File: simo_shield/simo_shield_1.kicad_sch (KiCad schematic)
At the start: 8 parts, among them J1 modulo_usb_debug, J2 conector_bateria, U1 modulo_flash_externa, U2 elemon_board, U3 bluepill_board_stm32, U4 modulo_acelerometro

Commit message: update en simo_bateria
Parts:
- J2: footprint Connector_JST:JST_EH_B2B-EH-A_1x02_P2.50mm_Vertical -> simo_shield:JST_EH_B2B-EH-A_1x02_P2.50mm_Vertical
- U1: footprint simo_board:conector_flash_ext -> simo_shield:conector_flash_ext
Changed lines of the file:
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@@
     (property "Reference" "U1" (id 0) (at 35.56 151.257 0))
     (property "Value" "modulo_flash_externa" (id 1) (at 35.56 153.797 0))
-    (property "Footprint" "simo_board:conector_flash_ext" (id 2) (at 48.26 156.972 0)
+    (property "Footprint" "simo_shield:conector_flash_ext" (id 2) (at 48.26 156.972 0)
       (effects (font (size 1.27 1.27)) hide)
     )
@@
       (effects (font (size 1.27 1.27)) (justify left))
     )
-    (property "Footprint" "Connector_JST:JST_EH_B2B-EH-A_1x02_P2.50mm_Vertical" (id 2) (at 243.967 108.458 0)
+    (property "Footprint" "simo_shield:JST_EH_B2B-EH-A_1x02_P2.50mm_Vertical" (id 2) (at 243.967 108.458 0)
       (effects (font (size 1.27 1.27)) hide)
     )
@@
     )
     (path "/aa8a4ce4-263f-4980-8d9f-4f0f7a62a8f5"
-      (reference "J2") (unit 1) (value "conector_bateria") (footprint "Connector_JST:JST_EH_B2B-EH-A_1x02_P2.50mm_Vertical")
+      (reference "J2") (unit 1) (value "conector_bateria") (footprint "simo_shield:JST_EH_B2B-EH-A_1x02_P2.50mm_Vertical")
     )
     (path "/50ab3c25-18ac-4348-9b10-e46fc412d281"
-      (reference "U1") (unit 1) (value "modulo_flash_externa") (footprint "simo_board:conector_flash_ext")
+      (reference "U1") (unit 1) (value "modulo_flash_externa") (footprint "simo_shield:conector_flash_ext")
     )
     (path "/4e546ac2-24a9-4fe8-8ba3-1b8a7c4f035f"

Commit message: update en ambas placas, revision 02
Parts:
- removed 155k1, 365k1: R, simo_shield:R_0805_2012Metric, symbol simo_shield:R
- removed U2: elemon_board, simo_shield:elemon_board, symbol simo_shield:elemon_board
- added U1: elemon_board, simo_shield:elemon_board, symbol simo_shield:elemon_board
- renumbered U1 to U2
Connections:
- net BAT_LEVEL is gone; now on an unnamed net: U3.25 (PA0)
- net BAT_ENA_PIN: now also U1.52 (BAT_ENA)
- net BAT_GND: now also U1.10 (GND)
- net GND_ELEMON: now also U3.41 (GND), U1.24 (GND)
- net UART_DEBUG_RX: now also U3.27 (PA2); no longer U3.28 (PA3)
- net UART_DEBUG_TX: now also U3.28 (PA3); no longer U3.27 (PA2)
- net USB33_ELEMON: now also U3.44 (3V3), U1.23 (USB33)
- net at U3.10 (PA15): now also U1.14 (RI)
- net at U3.7 (PA10): now also U1.2 (SER3_TX)
- net at U3.6 (PA9): now also U1.4 (SER3_RX)
- net at U3.2 (PB13): now also U1.9 (PWRKEY)
- no-connect marks 78 -> 76
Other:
- note added: "La tension en el conector es siempre menor a 3.3v"
- note removed: "0,30 * VBAT (8V MAX)"
- note removed: "ESTE PUENTE DEPENDE DE SI USAMOS 1 O DOS BATERIAS EN SERIE"
- moved on the sheet: J1, J2, U2, U3, U4

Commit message: update 2. Listo para revision 2
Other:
- note added: "La tension en el conector es siempre menor a 3.3v. PA0 canal analogico utilizado."
- note removed: "La tension en el conector es siempre menor a 3.3v"
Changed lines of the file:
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@@
   (junction (at 177.8 64.77) (diameter 0) (color 0 0 0 0)
-  )
-  (junction (at 217.17 100.33) (diameter 0) (color 0 0 0 0)
   )
   (junction (at 124.46 110.49) (diameter 0) (color 0 0 0 0)
@@
     (stroke (width 0) (type default) (color 0 0 0 0))
   )
-  (wire (pts (xy 173.99 100.33) (xy 217.17 100.33))
-    (stroke (width 0) (type default) (color 0 0 0 0))
-  )
   (wire (pts (xy 173.99 72.39) (xy 223.52 72.39))
     (stroke (width 0) (type default) (color 0 0 0 0))
@@
     (stroke (width 0) (type default) (color 0 0 0 0))
   )
-  (wire (pts (xy 217.17 99.06) (xy 217.17 100.33))
-    (stroke (width 0) (type default) (color 0 0 0 0))
-  )
   (polyline (pts (xy 283.21 40.64) (xy 283.21 83.82))
     (stroke (width 0) (type default) (color 0 0 0 0))
@@
     (stroke (width 0) (type default) (color 0 0 0 0))
   )
-  (wire (pts (xy 217.17 100.33) (xy 218.44 100.33))
+  (wire (pts (xy 173.99 100.33) (xy 218.44 100.33))
     (stroke (width 0) (type default) (color 0 0 0 0))
   )
@@
     (effects (font (size 1.27 1.27)) (justify left bottom))
   )
-  (text "La tension en el conector es siempre menor a 3.3v" (at 209.55 92.71 0)
+  (text "La tension en el conector es siempre menor a 3.3v.\nPA0 canal analogico utilizado."
+    (at 209.55 92.71 0)
     (effects (font (size 1.27 1.27)) (justify left bottom))
   )
@@
   (label "GND_ELEMON" (at 177.8 59.69 0)
     (effects (font (size 1.27 1.27)) (justify left bottom))
-  )
-  (symbol (lib_id "simo_shield:PWR_FLAG") (at 217.17 99.06 0) (unit 1)
-    (in_bom yes) (on_board yes)
-    (property "Reference" "#FLG01" (id 0) (at 217.17 97.155 0)
-      (effects (font (size 1.27 1.27)) hide)
-    )
-    (property "Value" "PWR_FLAG" (id 1) (at 217.17 95.25 0))
-    (property "Footprint" "" (id 2) (at 217.17 99.06 0)
-      (effects (font (size 1.27 1.27)) hide)
-    )
-    (property "Datasheet" "~" (id 3) (at 217.17 99.06 0)
-      (effects (font (size 1.27 1.27)) hide)
-    )
-    (pin "1")
   )
   (symbol (lib_id "simo_shield:modulo_flash_externa") (at 52.07 157.48 0) (mirror y) (unit 1)
@@
   )
   (symbol_instances
-    (path "/3bcc8c84-3847-43a1-a408-156ef3b78686"
-      (reference "#FLG01") (unit 1) (value "PWR_FLAG") (footprint "")
-    )
     (path "/fc6149f3-6c8e-44e2-b6f1-cd1c7ffb6984"
       (reference "J1") (unit 1) (value "modulo_usb_debug") (footprint "simo_shield:JST_EH_B2B-EH-A_1x02_P2.50mm_Vertical")

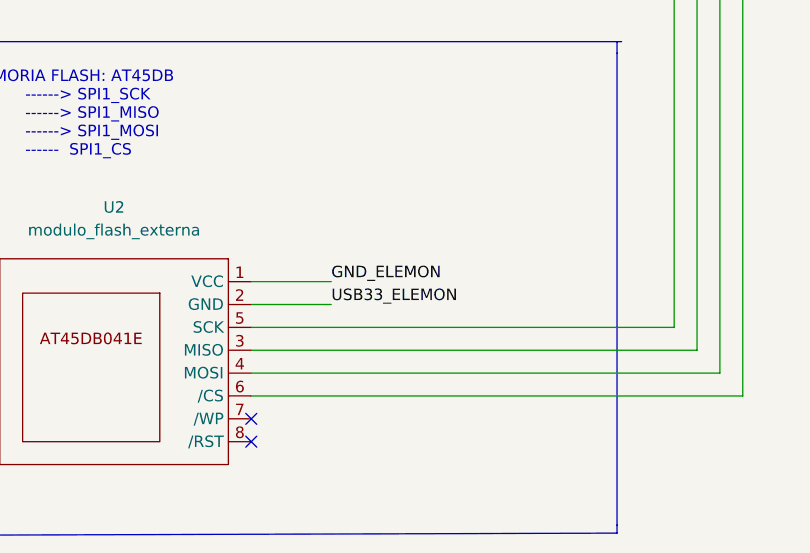
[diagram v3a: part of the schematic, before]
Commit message: modificaciones en simo_shield: modulo_flash_externo
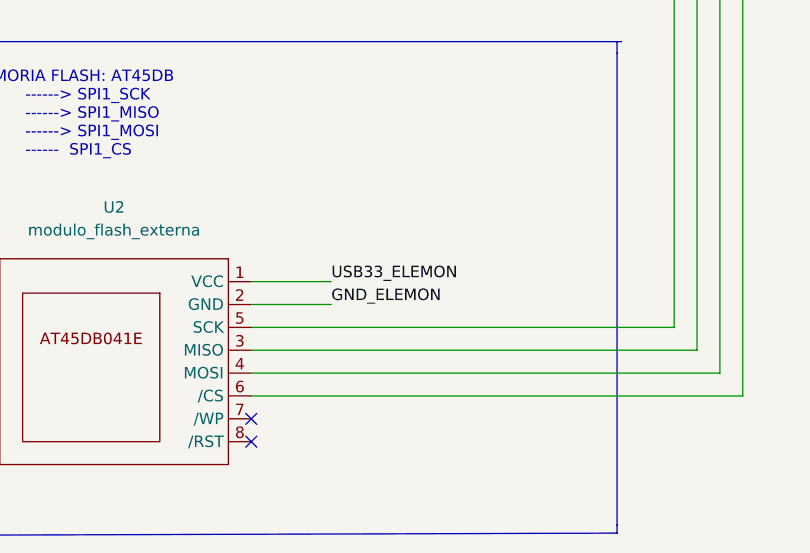
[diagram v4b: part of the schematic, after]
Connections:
- net GND_ELEMON: now also U2.2 (GND); no longer U2.1 (VCC)
- net USB33_ELEMON: now also U2.1 (VCC); no longer U2.2 (GND)
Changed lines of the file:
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@@
     (effects (font (size 1.27 1.27)) (justify right bottom))
   )
-  (label "GND_ELEMON" (at 63.5 160.02 0)
+  (label "GND_ELEMON" (at 63.5 162.56 0)
     (effects (font (size 1.27 1.27)) (justify left bottom))
   )
@@
     (effects (font (size 1.27 1.27)) (justify right bottom))
   )
-  (label "USB33_ELEMON" (at 63.5 162.56 0)
+  (label "USB33_ELEMON" (at 63.5 160.02 0)
     (effects (font (size 1.27 1.27)) (justify left bottom))
   )

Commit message: comenzamos el diseño del PCB de shield simo.
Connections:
- net at U1.14 (RI): now also U3.9 (PA12); no longer U3.10 (PA15)
- net at U1.9 (PWRKEY): now also U3.8 (PA11); no longer U3.2 (PB13)
- no-connect marks 76 -> 75
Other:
- note added: "ELEMON BOARD: BASADA EN SIM7000G PIN_SIM_ENA_BAT -------> PA1 (EN FIRMWARE ES PB12. MODIFICAR) PIN_SIM_PWRUP -------> PA11 (EN FIRMWARE ES PB13) PIN_AT_TX -------> PA10 PIN_AT_RX -------> PA9 PIN_RI -------> PA11"
- note removed: "ELEMON BOARD: BASADA EN SIM7000G PIN_SIM_ENA_BAT -------> PA1 (EN FIRMWARE ES PB12. MODIFICAR) PIN_SIM_PWRUP -------> PB13 PIN_AT_TX -------> PA10 PIN_AT_RX -------> PA9 PIN_RI -------> PA15"
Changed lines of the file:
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@@
   )
   (no_connect (at 127 69.85))
-  (no_connect (at 127 77.47))
   (no_connect (at 127 80.01))
   (no_connect (at 127 67.31))
@@
     (stroke (width 0) (type default) (color 0 0 0 0))
   )
+  (wire (pts (xy 127 77.47) (xy 101.6 77.47))
+    (stroke (width 0) (type default) (color 0 0 0 0))
+  )
   (wire (pts (xy 124.46 110.49) (xy 127 110.49))
     (stroke (width 0) (type default) (color 0 0 0 0))
@@
     (stroke (width 0) (type default) (color 0 0 0 0))
   )
+  (wire (pts (xy 101.6 77.47) (xy 101.6 62.23))
+    (stroke (width 0) (type default) (color 0 0 0 0))
+  )
   (wire (pts (xy 106.68 90.17) (xy 127 90.17))
     (stroke (width 0) (type default) (color 0 0 0 0))
@@
     (stroke (width 0) (type default) (color 0 0 0 0))
   )
-  (wire (pts (xy 67.31 62.23) (xy 127 62.23))
+  (wire (pts (xy 67.31 62.23) (xy 101.6 62.23))
     (stroke (width 0) (type default) (color 0 0 0 0))
   )
@@
     (effects (font (size 1.27 1.27)) (justify left bottom))
   )
-  (text "ELEMON BOARD: BASADA EN SIM7000G\n\nPIN_SIM_ENA_BAT    -------> PA1 (EN FIRMWARE ES PB12. MODIFICAR)\nPIN_SIM_PWRUP     -------> PB13\nPIN_AT_TX	     -------> PA10\nPIN_AT_RX	     -------> PA9\nPIN_RI			-------> PA15"
+  (text "ELEMON BOARD: BASADA EN SIM7000G\n\nPIN_SIM_ENA_BAT    -------> PA1 (EN FIRMWARE ES PB12. MODIFICAR)\nPIN_SIM_PWRUP     -------> PA11 (EN FIRMWARE ES PB13)\nPIN_AT_TX	     -------> PA10\nPIN_AT_RX	     -------> PA9\nPIN_RI			-------> PA11"
     (at 18.415 34.29 0)
     (effects (font (size 1.27 1.27)) (justify left bottom))

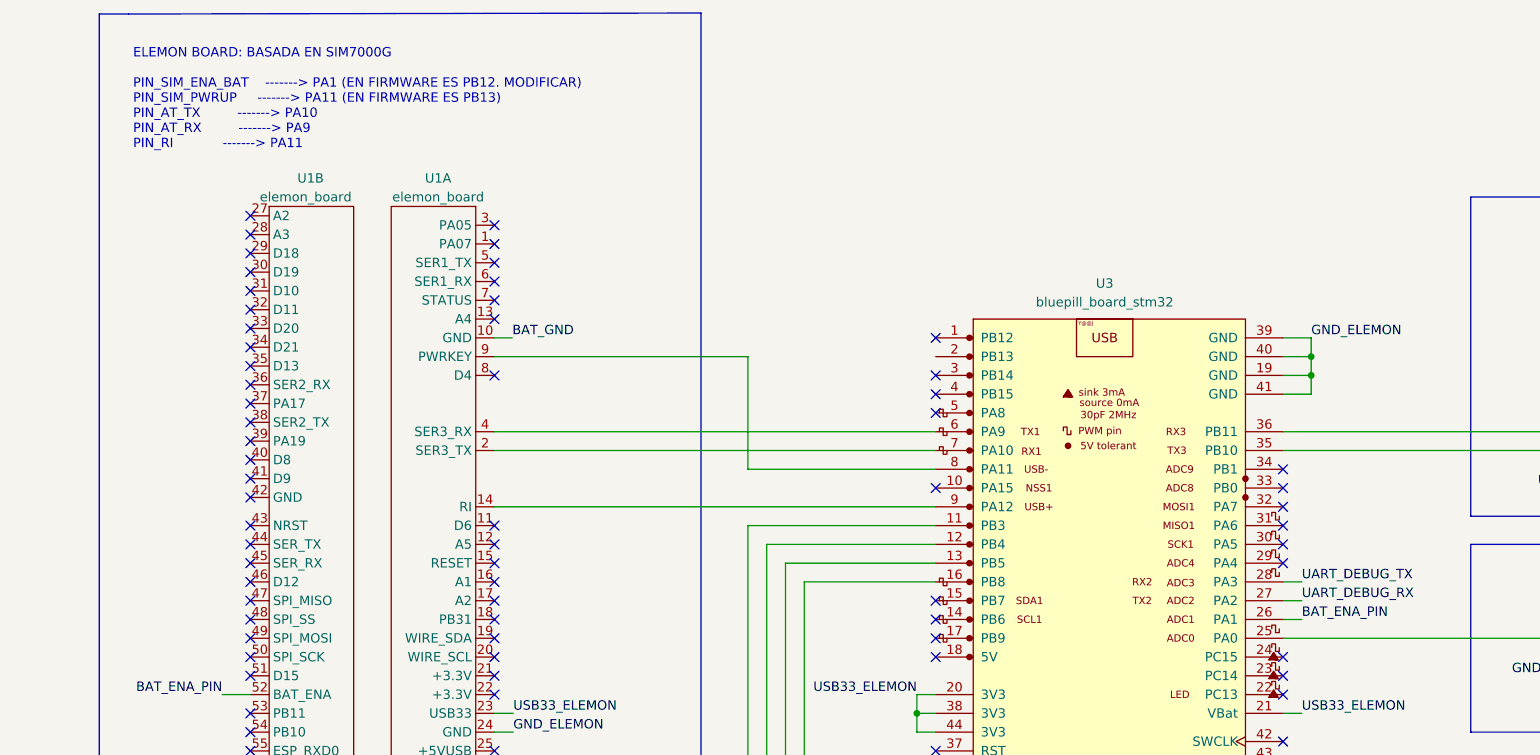
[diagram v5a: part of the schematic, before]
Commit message: simo shield: primer prototipo de pista terminado. 0 errores 26 warning. Todos por cortes en serigrafia
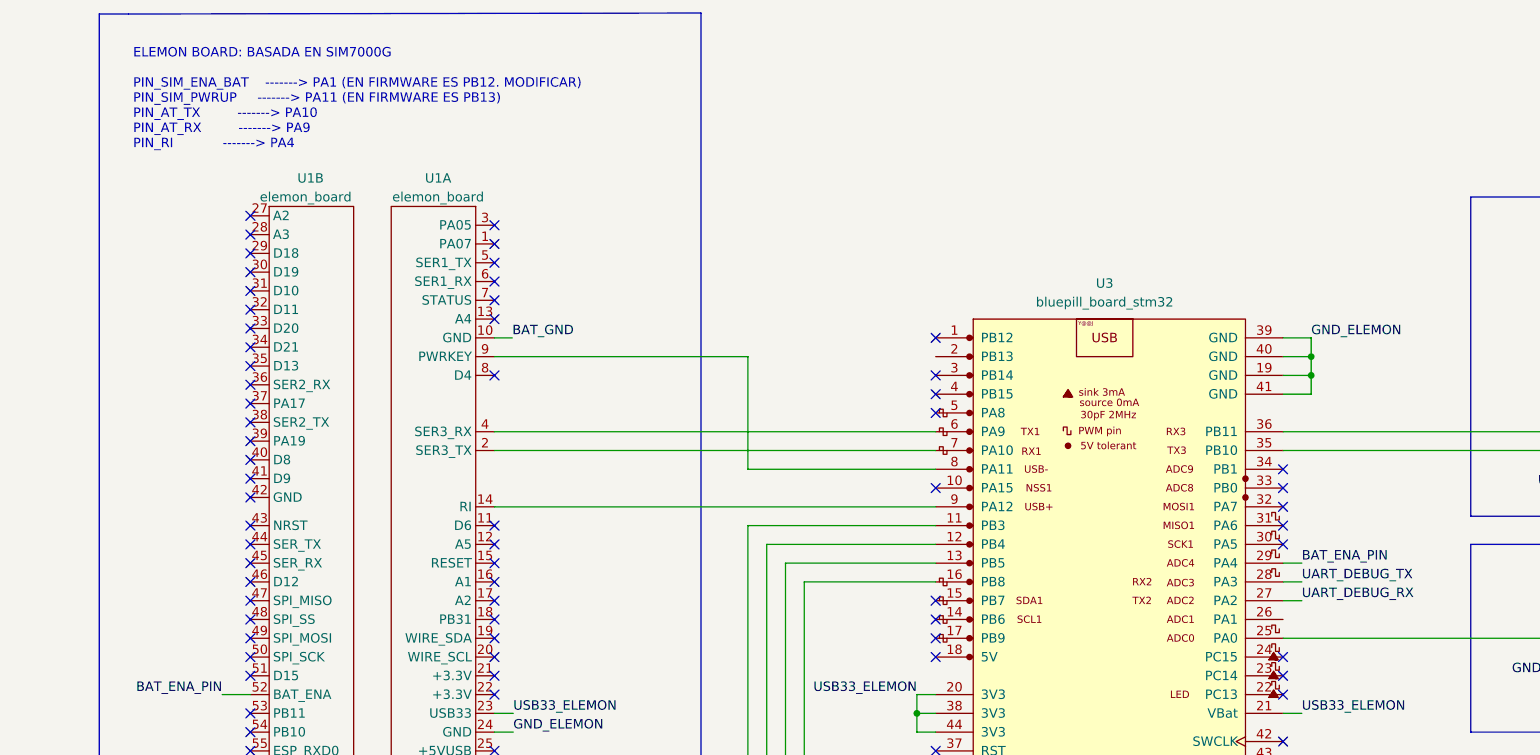
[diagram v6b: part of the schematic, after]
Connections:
- net BAT_ENA_PIN: now also U3.29 (PA4); no longer U3.26 (PA1)
- no-connect marks 75 -> 74
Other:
- note added: "ELEMON BOARD: BASADA EN SIM7000G PIN_SIM_ENA_BAT -------> PA1 (EN FIRMWARE ES PB12. MODIFICAR) PIN_SIM_PWRUP -------> PA11 (EN FIRMWARE ES PB13) PIN_AT_TX -------> PA10 PIN_AT_RX -------> PA9 PIN_RI -------> PA4"
- note removed: "ELEMON BOARD: BASADA EN SIM7000G PIN_SIM_ENA_BAT -------> PA1 (EN FIRMWARE ES PB12. MODIFICAR) PIN_SIM_PWRUP -------> PA11 (EN FIRMWARE ES PB13) PIN_AT_TX -------> PA10 PIN_AT_RX -------> PA9 PIN_RI -------> PA11"
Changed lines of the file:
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@@
   (no_connect (at 173.99 116.84))
   (no_connect (at 127 115.57))
-  (no_connect (at 173.99 90.17))
   (wire (pts (xy 173.99 110.49) (xy 176.53 110.49))
     (stroke (width 0) (type default) (color 0 0 0 0))
@@
     (stroke (width 0) (type default) (color 0 0 0 0))
   )
+  (wire (pts (xy 173.99 90.17) (xy 176.53 90.17))
+    (stroke (width 0) (type default) (color 0 0 0 0))
+  )
   (wire (pts (xy 173.99 95.25) (xy 176.53 95.25))
     (stroke (width 0) (type default) (color 0 0 0 0))
@@
   )
   (wire (pts (xy 173.99 67.31) (xy 177.8 67.31))
-    (stroke (width 0) (type default) (color 0 0 0 0))
-  )
-  (wire (pts (xy 173.99 97.79) (xy 176.53 97.79))
     (stroke (width 0) (type default) (color 0 0 0 0))
   )
@@
     (effects (font (size 1.27 1.27)) (justify left bottom))
   )
-  (text "ELEMON BOARD: BASADA EN SIM7000G\n\nPIN_SIM_ENA_BAT    -------> PA1 (EN FIRMWARE ES PB12. MODIFICAR)\nPIN_SIM_PWRUP     -------> PA11 (EN FIRMWARE ES PB13)\nPIN_AT_TX	     -------> PA10\nPIN_AT_RX	     -------> PA9\nPIN_RI			-------> PA11"
+  (text "ELEMON BOARD: BASADA EN SIM7000G\n\nPIN_SIM_ENA_BAT    -------> PA1 (EN FIRMWARE ES PB12. MODIFICAR)\nPIN_SIM_PWRUP     -------> PA11 (EN FIRMWARE ES PB13)\nPIN_AT_TX	     -------> PA10\nPIN_AT_RX	     -------> PA9\nPIN_RI			-------> PA4"
     (at 18.415 34.29 0)
     (effects (font (size 1.27 1.27)) (justify left bottom))
@@
     (effects (font (size 1.27 1.27)) (justify left bottom))
   )
-  (label "BAT_ENA_PIN" (at 176.53 97.79 0)
-    (effects (font (size 1.27 1.27)) (justify left bottom))
-  )
+  (label "BAT_ENA_PIN" (at 176.53 90.17 0)
+    (effects (font (size 1.27 1.27)) (justify left bottom))
+  )
